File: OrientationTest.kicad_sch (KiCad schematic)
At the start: 1 part

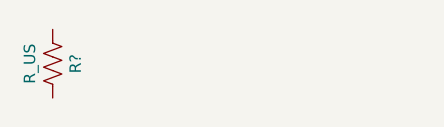
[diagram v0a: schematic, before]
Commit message: add non-symemtric part
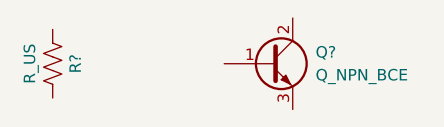
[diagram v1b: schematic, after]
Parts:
- added Q?: Q_NPN_BCE, symbol Device:Q_NPN_BCE
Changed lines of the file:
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@@
 (kicad_sch (version 20211123) (generator eeschema)
   (paper "A4")
+  (symbol (lib_id "Device:Q_NPN_BCE") (at 167.64 95.25 0) (unit 1)
+    (in_bom yes) (on_board yes)
+    (property "Reference" "Q?" (id 0) (at 172.72 93.98 0)
+      (effects (font (size 1.27 1.27)) (justify left))
+    )
+    (property "Value" "Q_NPN_BCE" (id 1) (at 172.72 96.52 0)
+      (effects (font (size 1.27 1.27)) (justify left))
+    )
+    (property "Footprint" "" (id 2) (at 172.72 92.71 0)
+      (effects (font (size 1.27 1.27)) hide)
+    )
+    (property "Datasheet" "~" (id 3) (at 167.64 95.25 0)
+      (effects (font (size 1.27 1.27)) hide)
+    )
+    (pin "1")
+    (pin "2")
+    (pin "3")
+  )
   (symbol (lib_id "Device:R_US") (at 143.51 95.25 0) (unit 1)
     (in_bom yes) (on_board yes)
@@
   )
   (symbol_instances
+    (path "/547ba58e-a9bf-429c-872c-80dcec988576"
+      (reference "Q?") (unit 1) (value "Q_NPN_BCE") (footprint "")
+    )
     (path "/6970d43d-2b0f-43c8-870d-b495541b9a1c"
       (reference "R?") (unit 1) (value "R_US") (footprint "")
